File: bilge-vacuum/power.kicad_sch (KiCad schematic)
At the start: 17 parts, among them Q10 Q_PMOS_GSD, Q7 Q_NMOS_GSD, Q8 Q_NMOS_GSD, U13 ADP151

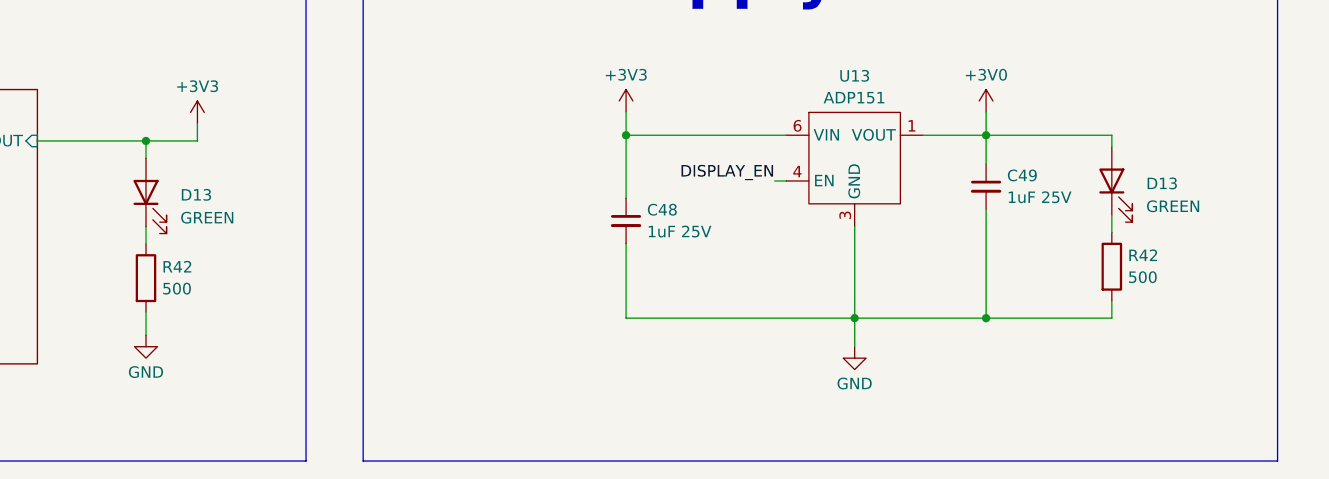
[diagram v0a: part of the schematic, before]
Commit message: Assign the bulk of parts, some passives still need custom footprints.
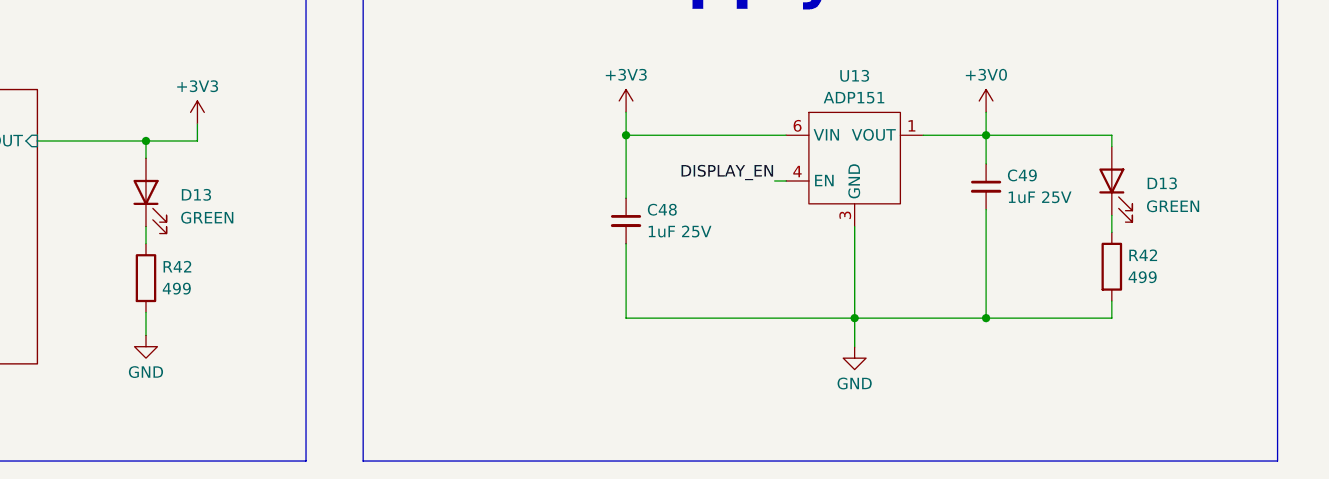
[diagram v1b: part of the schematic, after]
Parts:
- C48, C49: footprint (none) -> Capacitor_SMD:C_0805_2012Metric
- D13, D2, D3, D7: footprint (none) -> LED_SMD:LED_0805_2012Metric
- Q10, Q7, Q8: footprint (none) -> Package_TO_SOT_SMD:SOT-23-3
- R26, R45, R46, R47: footprint (none) -> Resistor_SMD:R_0805_2012Metric
- R42: value 500 -> 499; footprint (none) -> Resistor_SMD:R_0805_2012Metric
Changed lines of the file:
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@@
       (effects (font (size 1.27 1.27)) (justify right))
     )
-    (property "Footprint" "" (at 191.135 133.985 0)
+    (property "Footprint" "LED_SMD:LED_0805_2012Metric" (at 191.135 133.985 0)
       (effects (font (size 1.27 1.27)) hide)
     )
@@
       (effects (font (size 1.27 1.27)) (justify right))
     )
-    (property "Footprint" "" (at 120.65 50.8 0)
+    (property "Footprint" "LED_SMD:LED_0805_2012Metric" (at 120.65 50.8 0)
       (effects (font (size 1.27 1.27)) hide)
     )
@@
       (effects (font (size 1.27 1.27)))
     )
-    (property "Footprint" "" (at 153.035 55.245 0)
+    (property "Footprint" "Package_TO_SOT_SMD:SOT-23-3" (at 153.035 55.245 0)
       (effects (font (size 1.27 1.27)) hide)
     )
@@
       (effects (font (size 1.27 1.27)) (justify left))
     )
-    (property "Footprint" "" (at 137.16 138.43 0)
+    (property "Footprint" "Capacitor_SMD:C_0805_2012Metric" (at 137.16 138.43 0)
       (effects (font (size 1.27 1.27)) hide)
     )
@@
       (effects (font (size 1.27 1.27)) (justify left))
     )
-    (property "Footprint" "" (at 227.457 64.135 90)
+    (property "Footprint" "Resistor_SMD:R_0805_2012Metric" (at 227.457 64.135 90)
       (effects (font (size 1.27 1.27)) hide)
     )
@@
       (effects (font (size 1.27 1.27)) (justify left))
     )
-    (property "Footprint" "" (at 137.287 46.99 90)
+    (property "Footprint" "Resistor_SMD:R_0805_2012Metric" (at 137.287 46.99 90)
       (effects (font (size 1.27 1.27)) hide)
     )
@@
       (effects (font (size 1.27 1.27)) (justify left))
     )
-    (property "Value" "500" (at 192.913 144.7221 0)
-      (effects (font (size 1.27 1.27)) (justify left))
-    )
-    (property "Footprint" "" (at 189.357 143.51 90)
+    (property "Value" "499" (at 192.913 144.7221 0)
+      (effects (font (size 1.27 1.27)) (justify left))
+    )
+    (property "Footprint" "Resistor_SMD:R_0805_2012Metric" (at 189.357 143.51 90)
       (effects (font (size 1.27 1.27)) hide)
     )
@@
       (effects (font (size 1.27 1.27)) (justify right))
     )
-    (property "Footprint" "" (at 83.82 135.255 0)
+    (property "Footprint" "LED_SMD:LED_0805_2012Metric" (at 83.82 135.255 0)
       (effects (font (size 1.27 1.27)) hide)
     )
@@
       (effects (font (size 1.27 1.27)) (justify left))
     )
-    (property "Footprint" "" (at 97.155 61.595 0)
+    (property "Footprint" "Package_TO_SOT_SMD:SOT-23-3" (at 97.155 61.595 0)
       (effects (font (size 1.27 1.27)) hide)
     )
@@
       (effects (font (size 1.27 1.27)) (justify left))
     )
-    (property "Footprint" "" (at 123.19 68.58 0)
+    (property "Footprint" "Package_TO_SOT_SMD:SOT-23-3" (at 123.19 68.58 0)
       (effects (font (size 1.27 1.27)) hide)
     )
@@
       (effects (font (size 1.27 1.27)) (justify left))
     )
-    (property "Footprint" "" (at 177.165 134.62 0)
+    (property "Footprint" "Capacitor_SMD:C_0805_2012Metric" (at 177.165 134.62 0)
       (effects (font (size 1.27 1.27)) hide)
     )
@@
       (effects (font (size 1.27 1.27)))
     )
-    (property "Footprint" "" (at 148.717 73.025 90)
+    (property "Footprint" "Resistor_SMD:R_0805_2012Metric" (at 148.717 73.025 90)
       (effects (font (size 1.27 1.27)) hide)
     )
@@
       (effects (font (size 1.27 1.27)) (justify right))
     )
-    (property "Footprint" "" (at 229.235 53.34 0)
+    (property "Footprint" "LED_SMD:LED_0805_2012Metric" (at 229.235 53.34 0)
       (effects (font (size 1.27 1.27)) hide)
     )
@@
       (effects (font (size 1.27 1.27)) (justify right))
     )
-    (property "Footprint" "" (at 150.495 64.135 0)
+    (property "Footprint" "LED_SMD:LED_0805_2012Metric" (at 150.495 64.135 0)
       (effects (font (size 1.27 1.27)) hide)
     )
@@
       (effects (font (size 1.27 1.27)) (justify left))
     )
-    (property "Footprint" "" (at 118.872 60.325 90)
+    (property "Footprint" "Resistor_SMD:R_0805_2012Metric" (at 118.872 60.325 90)
       (effects (font (size 1.27 1.27)) hide)
     )
@@
       (effects (font (size 1.27 1.27)) (justify left))
     )
-    (property "Value" "500" (at 85.598 145.9921 0)
-      (effects (font (size 1.27 1.27)) (justify left))
-    )
-    (property "Footprint" "" (at 82.042 144.78 90)
-      (effects (font (size 1.27 1.27)) hide)
-    )
+    (property "Value" "499" (at 85.598 145.9921 0)
+      (effects (font (size 1.27 1.27)) (justify left))
+    )
+    (property "Footprint" "Resistor_SMD:R_0805_2012Metric" (at 82.042 144.78 90)
+      (effects (font (size 1.27 1.27)) hide)
+    )

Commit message: WIP
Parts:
- added J10: Screw_Terminal_01x02, Custom Parts:2604-1102, symbol Connector:Screw_Terminal_01x02
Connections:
- net GND: now also J10.2 (Pin_2)
- new net Input Protection/VIN: J10.1 (Pin_1)
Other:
- moved on the sheet: D2, D3, D7, Q10, Q7, Q8, R26, R45, R46, R47

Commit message: bilge vac 1v0
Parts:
- removed D13: GREEN, LED_SMD:LED_0805_2012Metric, symbol Device:LED
- removed R42: 499, Resistor_SMD:R_0805_2012Metric, symbol Device:R
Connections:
- net at U13.2 (NC): no longer U13.5 (NC)
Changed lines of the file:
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@@
   (junction (at 164.465 52.705) (diameter 0) (color 0 0 0 0)
   )
-  (junction (at 83.82 129.54) (diameter 0) (color 0 0 0 0)
-  )
   (junction (at 146.05 80.01) (diameter 0) (color 0 0 0 0)
   )
@@
     (stroke (width 0) (type default))
   )
-  (wire (pts (xy 39.37 133.985) (xy 43.815 133.985))
+  (wire (pts (xy 39.37 133.985) (xy 52.07 133.985))
     (stroke (width 0) (type default))
   )
@@
     (stroke (width 0) (type default))
   )
-  (wire (pts (xy 71.755 129.54) (xy 83.82 129.54))
-    (stroke (width 0) (type default))
-  )
   (wire (pts (xy 215.265 41.91) (xy 215.265 45.085))
     (stroke (width 0) (type default))
@@
     (stroke (width 0) (type default))
   )
-  (wire (pts (xy 83.82 129.54) (xy 89.535 129.54))
+  (wire (pts (xy 80.01 129.54) (xy 89.535 129.54))
     (stroke (width 0) (type default))
   )
@@
     (stroke (width 0) (type default))
   )
-  (wire (pts (xy 83.82 139.065) (xy 83.82 140.97))
-    (stroke (width 0) (type default))
-  )
   (wire (pts (xy 137.16 128.905) (xy 137.16 135.89))
     (stroke (width 0) (type default))
@@
     (stroke (width 0) (type default))
   )
-  (wire (pts (xy 83.82 129.54) (xy 83.82 131.445))
-    (stroke (width 0) (type default))
-  )
   (wire (pts (xy 164.465 50.8) (xy 164.465 52.705))
     (stroke (width 0) (type default))
@@
     (stroke (width 0) (type default))
   )
-  (wire (pts (xy 39.37 129.54) (xy 43.815 129.54))
+  (wire (pts (xy 39.37 129.54) (xy 52.07 129.54))
     (stroke (width 0) (type default))
   )
@@
   )
   (wire (pts (xy 154.94 133.985) (xy 153.67 133.985))
-    (stroke (width 0) (type default))
-  )
-  (wire (pts (xy 83.82 148.59) (xy 83.82 151.13))
     (stroke (width 0) (type default))
   )
@@
     )
   )
-  (symbol (lib_id "power:GND") (at 83.82 151.13 0) (unit 1)
-    (in_bom yes) (on_board yes) (dnp no) (fields_autoplaced)
-    (property "Reference" "#PWR040" (at 83.82 157.48 0)
-      (effects (font (size 1.27 1.27)) hide)
-    )
-    (property "Value" "GND" (at 83.82 155.2631 0)
-      (effects (font (size 1.27 1.27)))
-    )
-    (property "Footprint" "" (at 83.82 151.13 0)
-      (effects (font (size 1.27 1.27)) hide)
-    )
-    (property "Datasheet" "" (at 83.82 151.13 0)
-      (effects (font (size 1.27 1.27)) hide)
-    )
-    (pin "1")
-    (instances
-      (project "bilge-vacuum"
-        (path "/08405ba3-6912-4dc1-869a-b11176a5bc8a"
-          (reference "#PWR040") (unit 1)
-        )
-        (path "/08405ba3-6912-4dc1-869a-b11176a5bc8a/8a95e837-e0e7-4b78-93e7-7ab95e7c82dc"
-          (reference "#PWR015") (unit 1)
-        )
-      )
-    )
-  )
-  (symbol (lib_id "power:+3.3V") (at 208.915 41.91 0) (unit 1)
+  (symbol (lib_id "power:+3V3") (at 208.915 41.91 0) (unit 1)
     (in_bom yes) (on_board yes) (dnp no) (fields_autoplaced)
     (property "Reference" "#PWR028" (at 208.915 45.72 0)
       (effects (font (size 1.27 1.27)) hide)
     )
-    (property "Value" "+3.3V" (at 208.915 37.7769 0)
+    (property "Value" "+3V3" (at 208.915 38.354 0)
       (effects (font (size 1.27 1.27)))
     )
@@
         (path "/08405ba3-6912-4dc1-869a-b11176a5bc8a/8a95e837-e0e7-4b78-93e7-7ab95e7c82dc"
           (reference "R42") (unit 1)
-        )
-      )
-    )
-  )
-  (symbol (lib_id "Device:LED") (at 83.82 135.255 90) (unit 1)
-    (in_bom yes) (on_board yes) (dnp no) (fields_autoplaced)
-    (property "Reference" "D13" (at 87.63 135.5725 90)
-      (effects (font (size 1.27 1.27)) (justify right))
-    )
-    (property "Value" "GREEN" (at 87.63 138.1125 90)
-      (effects (font (size 1.27 1.27)) (justify right))
-    )
-    (property "Footprint" "LED_SMD:LED_0805_2012Metric" (at 83.82 135.255 0)
-      (effects (font (size 1.27 1.27)) hide)
-    )
-    (property "Datasheet" "~" (at 83.82 135.255 0)
-      (effects (font (size 1.27 1.27)) hide)
-    )
-    (pin "1")
-    (pin "2")
-    (instances
-      (project "bilge-vacuum"
-        (path "/08405ba3-6912-4dc1-869a-b11176a5bc8a"
-          (reference "D13") (unit 1)
-        )
-        (path "/08405ba3-6912-4dc1-869a-b11176a5bc8a/8a95e837-e0e7-4b78-93e7-7ab95e7c82dc"
-          (reference "D14") (unit 1)
         )
       )
@@
     )
   )
-  (symbol (lib_id "Device:R") (at 83.82 144.78 0) (unit 1)
-    (in_bom yes) (on_board yes) (dnp no) (fields_autoplaced)
-    (property "Reference" "R42" (at 85.598 143.5679 0)
-      (effects (font (size 1.27 1.27)) (justify left))
-    )
-    (property "Value" "499" (at 85.598 145.9921 0)
-      (effects (font (size 1.27 1.27)) (justify left))
-    )
-    (property "Footprint" "Resistor_SMD:R_0805_2012Metric" (at 82.042 144.78 90)
-      (effects (font (size 1.27 1.27)) hide)
-    )
-    (property "Datasheet" "~" (at 83.82 144.78 0)
-      (effects (font (size 1.27 1.27)) hide)
-    )
-    (pin "1")
-    (pin "2")
-    (instances
-      (project "bilge-vacuum"
-        (path "/08405ba3-6912-4dc1-869a-b11176a5bc8a"
-          (reference "R42") (unit 1)
-        )
-        (path "/08405ba3-6912-4dc1-869a-b11176a5bc8a/8a95e837-e0e7-4b78-93e7-7ab95e7c82dc"
-          (reference "R48") (unit 1)
-        )
-      )
-    )
-  )
   (sheet (at 219.075 40.005) (size 29.845 31.75) (fields_autoplaced)
     (stroke (width 0.1524) (type solid))
@@
     )
   )
-  (sheet (at 43.815 123.825) (size 27.94 30.48) (fields_autoplaced)
+  (sheet (at 52.07 123.825) (size 27.94 30.48) (fields_autoplaced)
     (stroke (width 0.1524) (type solid))
     (fill (color 0 0 0 0.0000))
-    (property "Sheetname" "3.3V Buck" (at 43.815 123.1134 0)
+    (property "Sheetname" "3.3V Buck" (at 52.07 123.1134 0)
       (effects (font (size 1.27 1.27)) (justify left bottom))
     )
-    (property "Sheetfile" "3v3_buck.kicad_sch" (at 43.815 154.8896 0)
+    (property "Sheetfile" "3v3_buck.kicad_sch" (at 52.07 154.8896 0)
       (effects (font (size 1.27 1.27)) (justify left top))
     )
-    (pin "3V3_OUT" input (at 71.755 129.54 0)
-      (effects (font (size 1.27 1.27)) (justify right))
-    )
-    (pin "VIN" input (at 43.815 129.54 180)
-      (effects (font (size 1.27 1.27)) (justify left))
-    )
-    (pin "ENABLE" input (at 43.815 133.985 180)
-      (effects (font (size 1.27 1.27)) (justify left))
-    )
+    (pin "3V3_OUT" input (at 80.01 129.54 0)
+      (effects (font (size 1.27 1.27)) (justify right))
+    )
+    (pin "VIN" input (at 52.07 129.54 180)
+      (effects (font (size 1.27 1.27)) (justify left))
+    )
+    (pin "ENABLE" input (at 52.07 133.985 180)
+      (effects (font (size 1.27 1.27)) (justify left))
+    )

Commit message: Fixes
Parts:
- removed Q8: Q_NMOS_GSD, Package_TO_SOT_SMD:SOT-23-3, symbol Device:Q_NMOS_GSD
- removed R47: 16k, Resistor_SMD:R_0805_2012Metric, symbol Device:R
- added Q10: Q_PMOS_GSD, Package_TO_SOT_SMD:SOT-23-3, symbol Device:Q_PMOS_GSD
- R26: value 2.2k -> 10k 1%
- R45, R46: value 2.61k -> 5k 1%
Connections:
- net +12V: now also Q10.2 (S); no longer D2.2 (A)
- net GND: now also R45.2
- net Input Protection/~{PGOOD}: now also Q10.1 (G)
- net DISPLAY_EN renamed DISP_3V0_ENABLE
- new net: D2.2 (A), Q10.3 (D)
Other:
- moved on the sheet: C48, D2, R45
